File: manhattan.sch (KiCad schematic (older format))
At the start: 111 parts, among them J1 USB, J2 MICROSD-JT10, K1 CONN_3, K2 CONN_3, K3 CONN_3, K4 CONN_3, P1 CONN_2, P2 CONN_2, P3 CONN_2, P5 CONN_7X2, Q1 MOSFET_N, Q2 MOSFET_N, Q3 MOSFET_N, U1 MC78M05CDTX, U2 AP7313, U3 TXB0104, X1 16.000

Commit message: Annotation
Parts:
- renumbered ICSP to ICSP1

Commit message: Arduino circuit for auto-selecting power source FDN430P pFET schematic
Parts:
- removed D1: LED, symbol LED
- removed ISP1: CONN_3X2, symbol CONN_3X2
- removed J1: USB, symbol USB
- removed K1, K2, K3, K4: CONN_3, symbol CONN_3
- removed P5: CONN_7X2, symbol CONN_7X2
- removed R12: R, symbol R
- removed USBPWR1: JUMPER, symbol JUMPER
- added D?: DIODE, symbol DIODE
- added P? (x5): CONN_2, symbol CONN_2
- added P?: CONN_8X2, symbol CONN_8X2
- added R? (x2): 10K, symbol R
- added T?: FDN340P, symbol FDN340P
- added U?: MICROUSB, symbol MICROUSB
- added U?: LM358, symbol LM358
- renumbered Z-DRIVER2 to E-DRIVER1
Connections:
- net labels added: RESET\, USBVCC
- wire segments 466 -> 467
- no-connect marks 8 -> 7
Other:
- note added: "5V"
- note removed: "ISP"
- moved on the sheet: C25, C27, C28, DP1, F1, ICSP1, P2, R18, R19, R20, R21, U1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

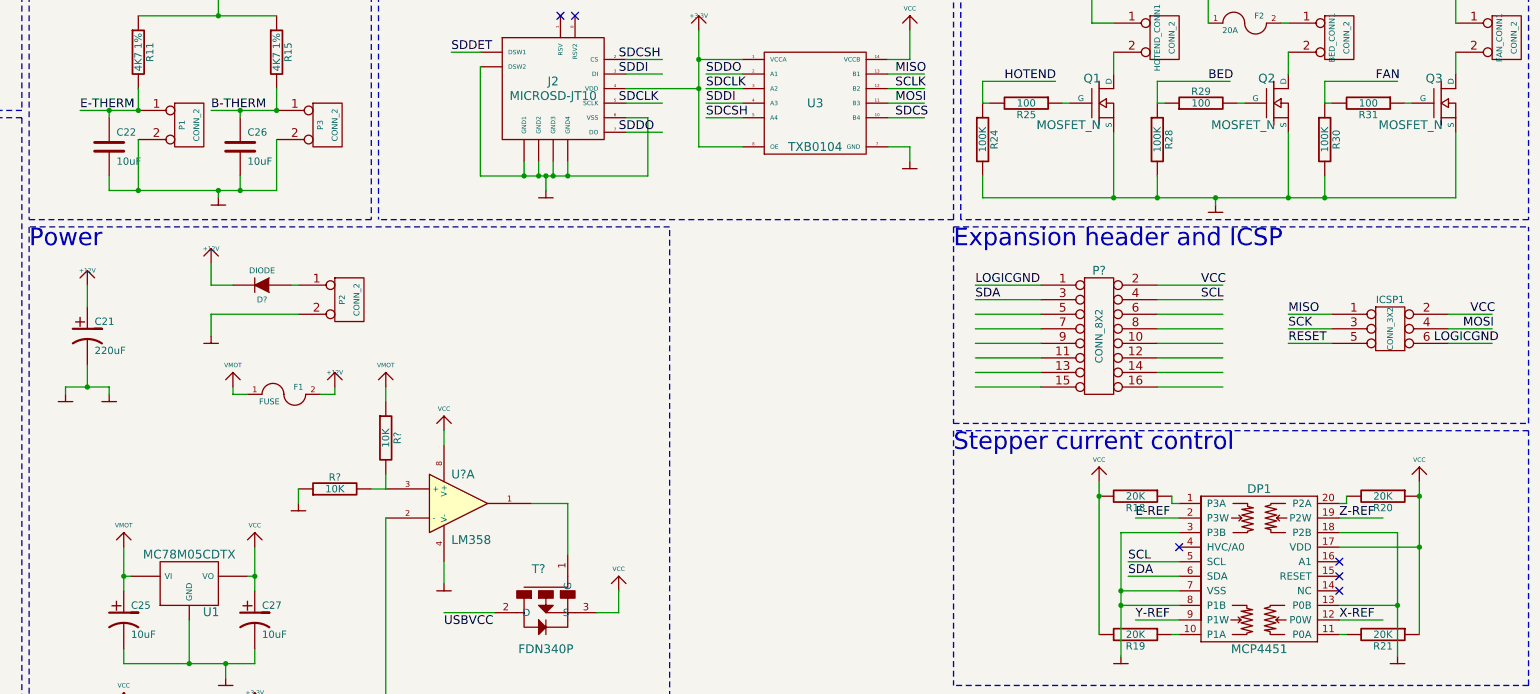
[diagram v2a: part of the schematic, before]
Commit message: Move a diode in power module; changed MOSFET driving circuit
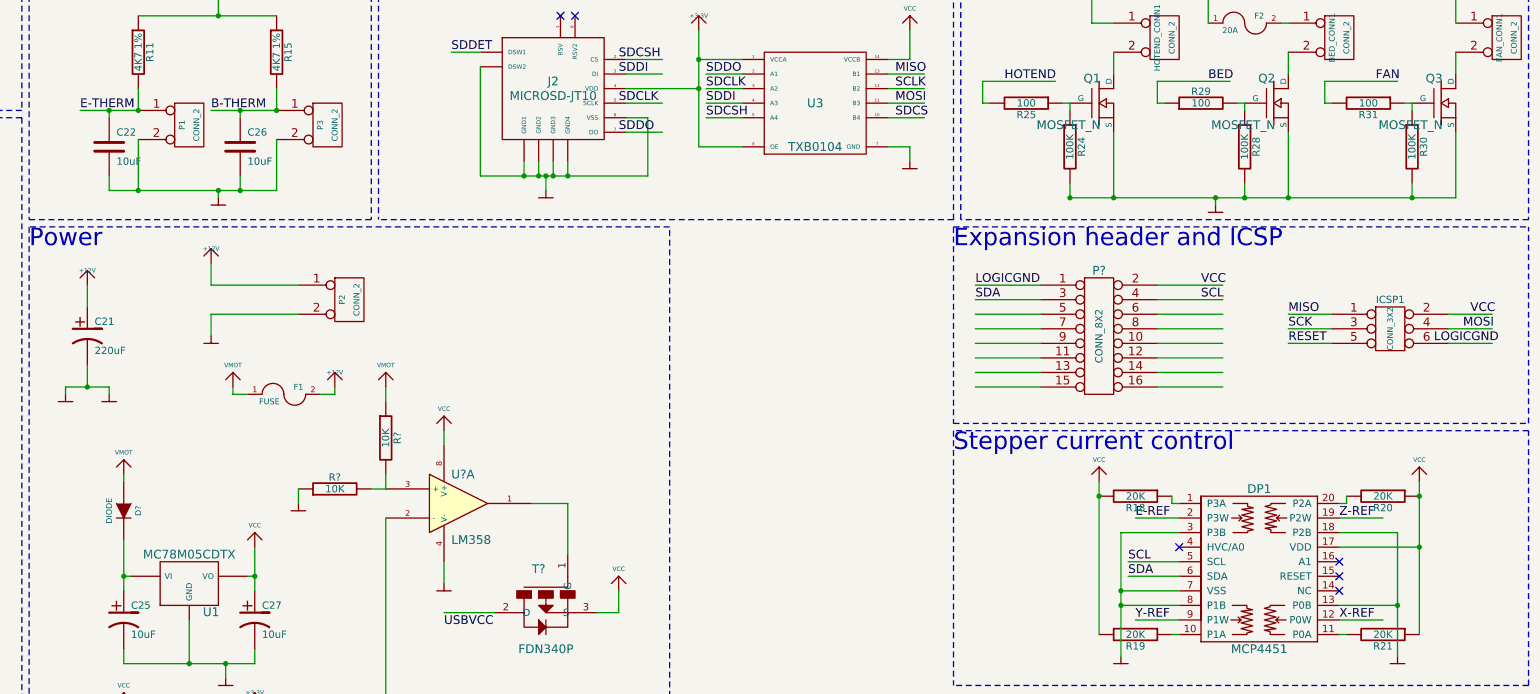
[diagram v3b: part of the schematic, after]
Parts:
- removed D?: DIODE, symbol DIODE
- added D?: DIODE, symbol DIODE
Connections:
- wire segments 467 -> 470
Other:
- moved on the sheet: R24, R28, R30
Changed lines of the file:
@@
-EESchema Schematic File Version 2  date Sun 22 Apr 2012 10:06:44 AM EDT
+EESchema Schematic File Version 2  date Fri 11 May 2012 01:42:47 PM EDT
 LIBS:manhattan
 LIBS:power
@@
 Sheet 1 1
 Title ""
-Date "22 apr 2012"
+Date "11 may 2012"
 Rev ""
 Comp ""
@@
 $EndDescr
 Wire Wire Line
+	6800 8100 6800 8450
+Wire Wire Line
+	8000 6350 7400 6350
+Connection ~ 15650 5750
+Wire Wire Line
+	15650 5650 15650 5750
+Connection ~ 14500 5750
+Wire Wire Line
+	14500 5650 14500 5750
+Wire Wire Line
+	13300 5150 13300 5100
+Wire Wire Line
 	8600 7150 8600 7050
 Wire Wire Line
@@
 Wire Wire Line
 	12650 7050 13100 7050
-Wire Wire Line
-	7550 6350 7400 6350
 Wire Wire Line
 	8150 7100 8250 7100
@@
 	12550 5900 12550 4100
 Wire Wire Line
-	15050 5750 15050 5600
-Connection ~ 13900 5750
-Wire Wire Line
-	13900 5600 13900 5750
-Wire Wire Line
 	14300 5750 14300 5800
 Wire Wire Line
-	12700 5600 12700 5750
-Wire Wire Line
 	14400 4950 13900 4950
 Wire Wire Line
@@
 	15100 5100 15050 5100
 Wire Wire Line
-	13250 5100 13300 5100
+	13300 5100 13250 5100
 Wire Wire Line
 	14450 5100 14500 5100
@@
 	6800 9450 6800 9250
 Connection ~ 6800 8350
-Wire Wire Line
-	6800 8450 6800 8150
 Wire Wire Line
 	7400 6700 7400 6550
@@
 Connection ~ 14300 5750
 Wire Wire Line
-	12700 5750 15950 5750
-Wire Wire Line
-	15950 5750 15950 5300
-Connection ~ 15050 5750
+	15950 5300 15950 5750
 Wire Wire Line
 	5400 9800 5150 9800
@@
 	1350 7550 1350 7500
 Wire Wire Line
-	7950 6350 8000 6350
-Wire Wire Line
 	7400 6550 8000 6550
 Wire Wire Line
@@
 Wire Wire Line
 	8600 7750 8600 7650
+Wire Wire Line
+	13300 5650 13300 5750
+Connection ~ 13300 5750
+Wire Wire Line
+	14500 5100 14500 5150
+Wire Wire Line
+	15650 5100 15650 5150
+Wire Wire Line
+	13300 5750 15950 5750
+Wire Wire Line
+	6800 7700 6800 7650
+$Comp
+L DIODE D?
+U 1 1 4FAAB613
+P 6800 7900
+F 0 "D?" H 6800 8000 40  0000 C CNN
+F 1 "DIODE" H 6800 7800 40  0000 C CNN
+	1    6800 7900
+	0    1    1    0
+$EndComp
 $Comp
 L LOGICGND #PWR?
@@
 	1    13500 6700
 	1    0    0    -1
-$EndComp
-$Comp
-L DIODE D?
-U 1 1 4F7FAB14
-P 7750 6350
-F 0 "D?" H 7750 6450 40  0000 C CNN
-F 1 "DIODE" H 7750 6250 40  0000 C CNN
-	1    7750 6350
-	-1   0    0    1
 $EndComp
 NoConn ~ 1650 7500
@@
 L R R30
 U 1 1 4F5BB1E0
-P 15050 5350
-F 0 "R30" V 15130 5350 50  0000 C CNN
-F 1 "100K" V 15050 5350 50  0000 C CNN
-	1    15050 5350
+P 15650 5400
+F 0 "R30" V 15730 5400 50  0000 C CNN
+F 1 "100K" V 15650 5400 50  0000 C CNN
+	1    15650 5400
 	1    0    0    -1
 $EndComp
@@
 L R R28
 U 1 1 4F5BB1DD
-P 13900 5350
-F 0 "R28" V 13980 5350 50  0000 C CNN
-F 1 "100K" V 13900 5350 50  0000 C CNN
-	1    13900 5350
+P 14500 5400
+F 0 "R28" V 14580 5400 50  0000 C CNN
+F 1 "100K" V 14500 5400 50  0000 C CNN
+	1    14500 5400
 	1    0    0    -1
 $EndComp
@@
 L R R24
 U 1 1 4F5BB1D7
-P 12700 5350
-F 0 "R24" V 12780 5350 50  0000 C CNN
-F 1 "100K" V 12700 5350 50  0000 C CNN
-	1    12700 5350
+P 13300 5400
+F 0 "R24" V 13380 5400 50  0000 C CNN
+F 1 "100K" V 13300 5400 50  0000 C CNN
+	1    13300 5400
 	1    0    0    -1
 $EndComp
@@
 L VMOT #PWR26
 U 1 1 4F5B9BC0
-P 6800 8150
-F 0 "#PWR26" H 6800 8300 30  0001 C CNN
-F 1 "VMOT" H 6800 8300 30  0000 C CNN
-	1    6800 8150
-	1    0    0    -1
-$EndComp
+P 6800 7650
+F 0 "#PWR26" H 6800 7800 30  0001 C CNN
+F 1 "VMOT" H 6800 7800 30  0000 C CNN
+	1    6800 7650
+	1    0    0    -1
+$EndComp

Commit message: First draft of board layout
- Changed some annotations
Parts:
- gave numbers to parts that had none: 12
- renumbered X-DRIVER1 to DRV1, Y-DRIVER1 to DRV2, Z-DRIVER1 to DRV3, E-DRIVER1 to DRV4, X-CONN1 to ST1, P1 to ST13, P3 to ST14, Y-CONN1 to ST2, Z-CONN1 to ST3, E0-CONN1 to ST4, P2 to ST5, HOTEND_CONN1 to ST6, BED_CONN1 to ST7, FAN_CONN1 to ST8
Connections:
- wire segments 470 -> 471

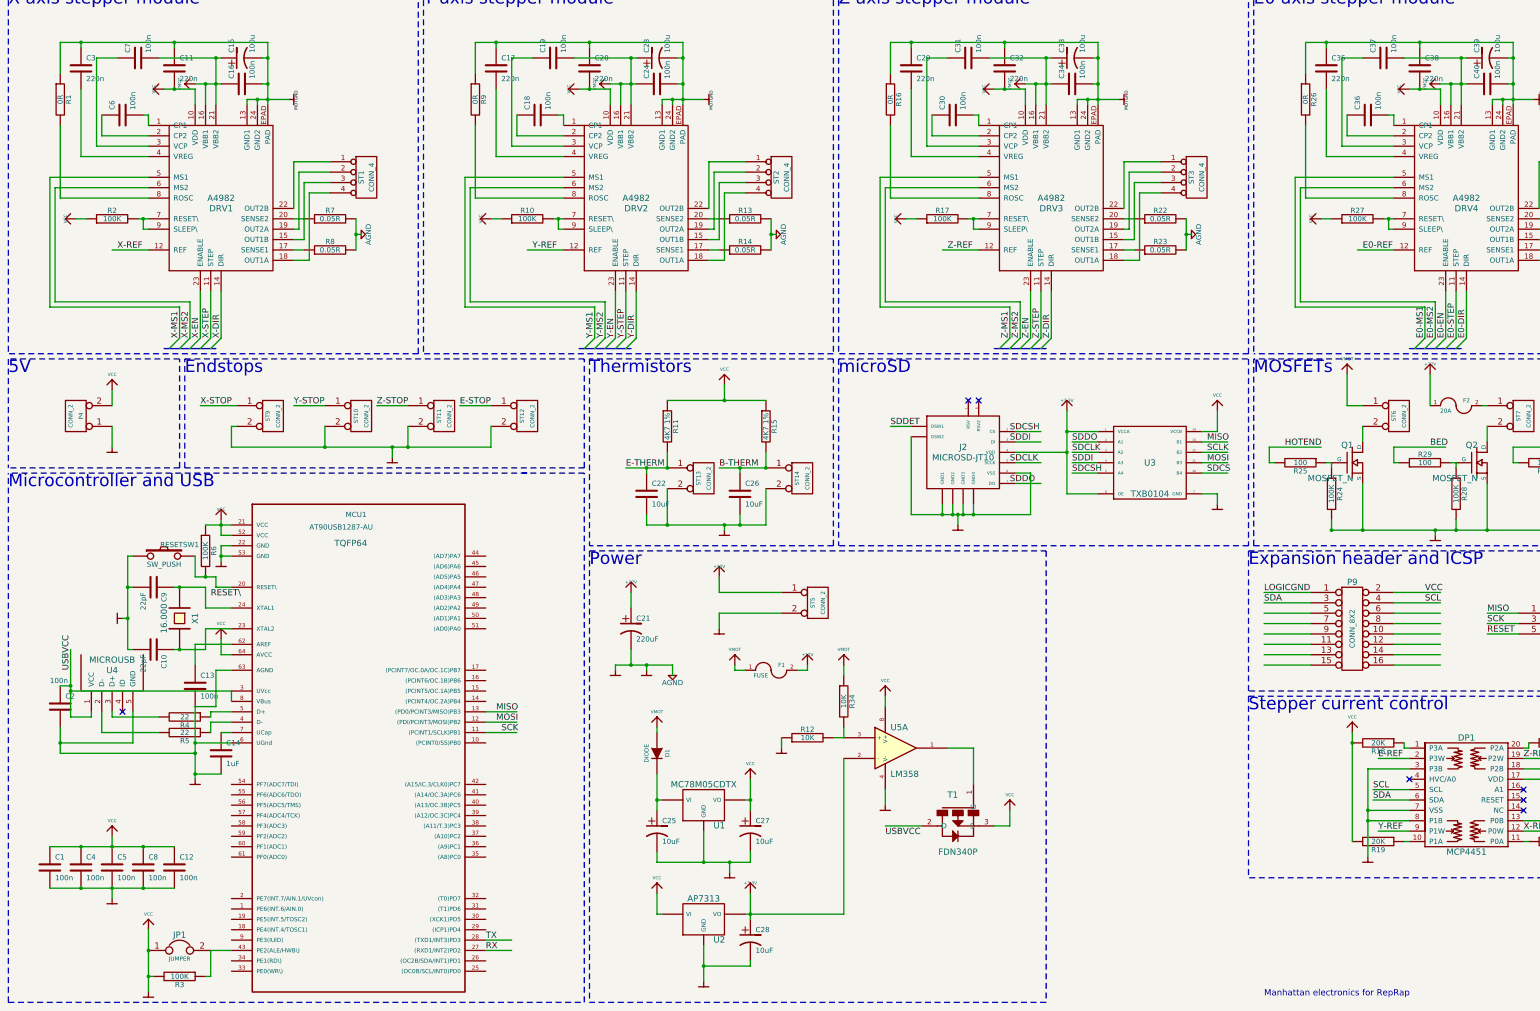
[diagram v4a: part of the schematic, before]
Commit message: Changed MS1/MS2 on stepper drivers
They are no longer connected to microcontroller pins, instead they will
pulled high by default, and the user can pull them down with a jumper.

Also fixed pulldown on HWB.
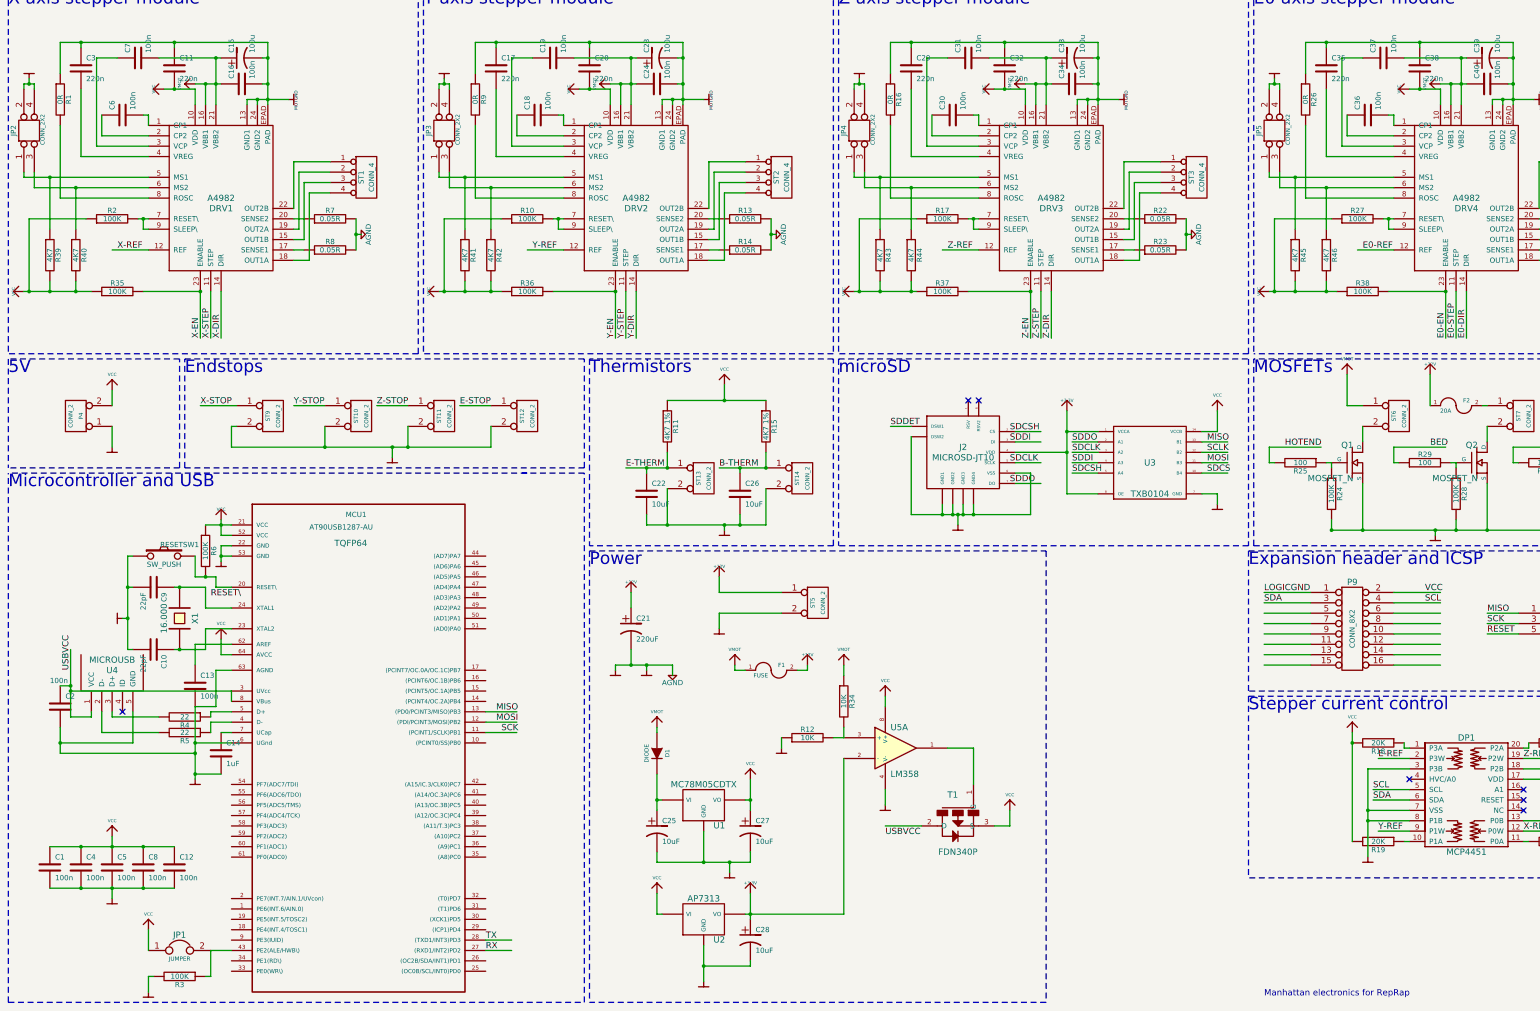
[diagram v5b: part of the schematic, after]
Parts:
- added JP2, JP3, JP4, JP5: CONN_2X2, symbol CONN_2X2
- added R35, R36, R37, R38: 100K, symbol R
- added R39, R40, R41, R42, R43, R44, R45, R46: 4K7, symbol R
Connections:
- net labels removed: E0-MS1, E0-MS2, X-MS1, X-MS2, Y-MS1, Y-MS2, Z-MS1, Z-MS2
- wire segments 471 -> 500

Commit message: Initial placement of power side of X stepper module
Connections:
- wire segments 500 -> 505

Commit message: Last version before dual extruder
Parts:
- removed ST12: CONN_2, symbol CONN_2
- added ST?: CONN_2, symbol CONN_2
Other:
- moved on the sheet: F1
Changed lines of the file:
@@
-EESchema Schematic File Version 2  date Sun 13 May 2012 01:23:53 PM EDT
+EESchema Schematic File Version 2  date Thu 17 May 2012 11:12:53 AM EDT
 LIBS:manhattan
 LIBS:power
@@
 Sheet 1 1
 Title ""
-Date "13 may 2012"
+Date "17 may 2012"
 Rev ""
 Comp ""
@@
 Comment4 ""
 $EndDescr
+Wire Wire Line
+	5300 4950 5300 4750
+Wire Wire Line
+	5300 4950 2700 4950
 Connection ~ 2750 2250
 Wire Wire Line
@@
 	2950 1600 2950 1900
 Wire Wire Line
-	2900 1900 2950 1900
+	2950 1900 2900 1900
 Wire Wire Line
 	2900 1900 2900 2250
@@
 Connection ~ 2850 2250
 Wire Wire Line
-	2700 2250 2900 2250
+	2900 2250 2700 2250
 Wire Wire Line
 	3650 2400 3450 2400
@@
 	12650 7050 13100 7050
 Wire Wire Line
-	8150 7100 8250 7100
-Wire Wire Line
-	8250 7100 8250 7050
+	9350 6600 9450 6600
+Wire Wire Line
+	9450 6600 9450 6550
 Connection ~ 1050 7800
 Wire Wire Line
@@
 	4250 4950 4250 5050
 Wire Wire Line
-	2700 4750 2700 4950
+	2700 4950 2700 4750
 Wire Wire Line
 	2700 4750 2750 4750
@@
 	3600 4750 3600 4950
 Connection ~ 3600 4950
-Wire Wire Line
-	5200 4750 5200 4950
-Wire Wire Line
-	5200 4950 2700 4950
 Connection ~ 4400 4950
 Wire Wire Line
 	3300 4550 3600 4550
-Wire Wire Line
-	5200 4550 4900 4550
 Wire Wire Line
 	6900 5000 6900 5150
@@
 	14800 5750 14800 5300
 Wire Wire Line
-	7650 7100 7550 7100
-Wire Wire Line
-	7550 7100 7550 7050
+	8850 6600 8750 6600
+Wire Wire Line
+	8750 6600 8750 6550
 Wire Wire Line
 	6550 6500 6550 6350
@@
 	2700 2200 2900 2200
 Connection ~ 2850 2200
+Wire Wire Line
+	4900 4550 5300 4550
+Text Label 4900 4550 0    60   ~ 0
+E-STOP
+$Comp
+L CONN_2 ST?
+U 1 1 4FB51527
+P 5650 4650
+F 0 "ST?" V 5600 4650 40  0000 C CNN
+F 1 "CONN_2" V 5700 4650 40  0000 C CNN
+	1    5650 4650
+	1    0    0    -1
+$EndComp
 $Comp
 L LOGICGND #PWR01
@@
 	1    1200 4650
 	-1   0    0    1
-$EndComp
-$Comp
-L CONN_2 ST12
-U 1 1 4F7FA873
-P 5550 4650
-F 0 "ST12" V 5500 4650 40  0000 C CNN
-F 1 "CONN_2" V 5600 4650 40  0000 C CNN
-	1    5550 4650
-	1    0    0    -1
 $EndComp
 $Comp
@@
 L +12V #PWR022
 U 1 1 4F5E720A
-P 8250 7050
-F 0 "#PWR022" H 8250 7000 20  0001 C CNN
-F 1 "+12V" H 8250 7150 30  0000 C CNN
-	1    8250 7050
+P 9450 6550
+F 0 "#PWR022" H 9450 6500 20  0001 C CNN
+F 1 "+12V" H 9450 6650 30  0000 C CNN
+	1    9450 6550
 	1    0    0    -1
 $EndComp
@@
 L FUSE F1
 U 1 1 4F5E4AA4
-P 7900 7100
-F 0 "F1" H 8000 7150 40  0000 C CNN
-F 1 "FUSE" H 7800 7050 40  0000 C CNN
-	1    7900 7100
+P 9100 6600
+F 0 "F1" H 9200 6650 40  0000 C CNN
+F 1 "FUSE" H 9000 6550 40  0000 C CNN
+	1    9100 6600
 	1    0    0    -1
 $EndComp
@@
 L VMOT #PWR024
 U 1 1 4F5E4AA0
-P 7550 7050
-F 0 "#PWR024" H 7550 7200 30  0001 C CNN
-F 1 "VMOT" H 7550 7200 30  0000 C CNN
-	1    7550 7050
+P 8750 6550
+F 0 "#PWR024" H 8750 6700 30  0001 C CNN
+F 1 "VMOT" H 8750 6700 30  0000 C CNN
+	1    8750 6550
 	1    0    0    -1
 $EndComp
@@
 Text Notes 2250 4250 0    120  ~ 0
 Endstops
-Text Label 4900 4550 0    60   ~ 0
-E-STOP
 Text Label 4100 4550 0    60   ~ 0
 Z-STOP
